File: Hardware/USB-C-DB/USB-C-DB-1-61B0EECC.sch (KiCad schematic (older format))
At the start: 5 parts

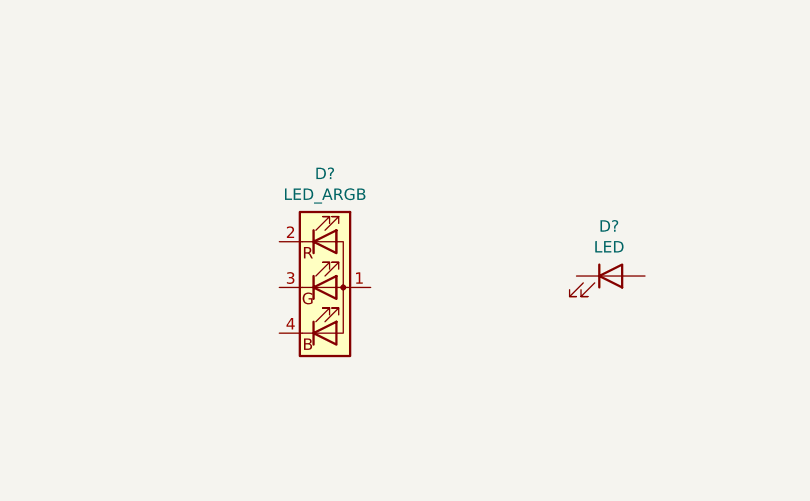
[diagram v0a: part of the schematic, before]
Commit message: Wiring up USB interface (schematic v0.3) > Adding ESD circuity for USB interface > Adding remaining bias and configuration circuity for the UBS interface IC
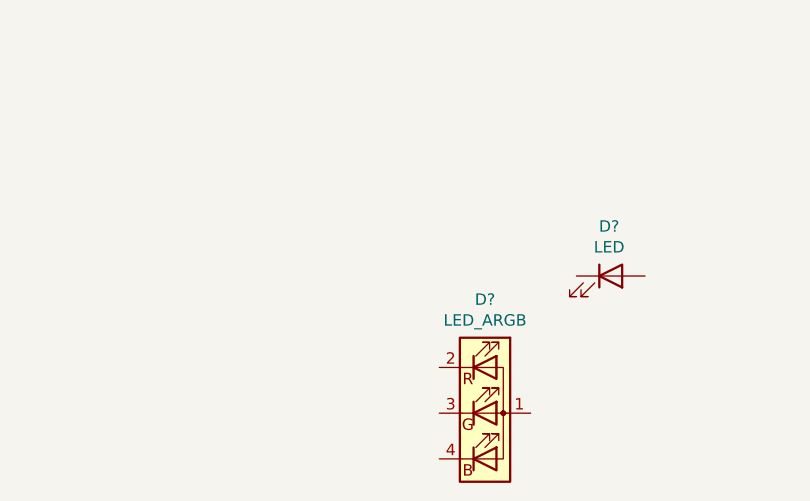
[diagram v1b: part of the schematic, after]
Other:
- moved on the sheet: D?
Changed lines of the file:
@@
 L Device:LED_ARGB D?
 U 1 1 61B13687
-P 4250 5550
+P 4950 6100
 AR Path="/61B13687" Ref="D?"  Part="1"
 AR Path="/61B0EECD/61B13687" Ref="D?"  Part="1"
-F 0 "D?" H 4250 6047 50  0000 C CNN
-F 1 "LED_ARGB" H 4250 5956 50  0000 C CNN
-F 2 "LED_SMD:LED_Cree-PLCC4_3.2x2.8mm_CCW" H 4250 5500 50  0001 C CNN
-F 3 "https://www.mouser.in/datasheet/2/723/CLV1L_FKB_1238-2583652.pdf" H 4250 5500 50  0001 C CNN
-F 4 "CLV1L-FKB-CJ1N1E1BB7B3B3" H 4250 5550 50  0001 C CNN "MPN"
-	1    4250 5550
+F 0 "D?" H 4950 6597 50  0000 C CNN
+F 1 "LED_ARGB" H 4950 6506 50  0000 C CNN
+F 2 "LED_SMD:LED_Cree-PLCC4_3.2x2.8mm_CCW" H 4950 6050 50  0001 C CNN
+F 3 "https://www.mouser.in/datasheet/2/723/CLV1L_FKB_1238-2583652.pdf" H 4950 6050 50  0001 C CNN
+F 4 "CLV1L-FKB-CJ1N1E1BB7B3B3" H 4950 6100 50  0001 C CNN "MPN"
+	1    4950 6100
 	1    0    0    -1
 $EndComp

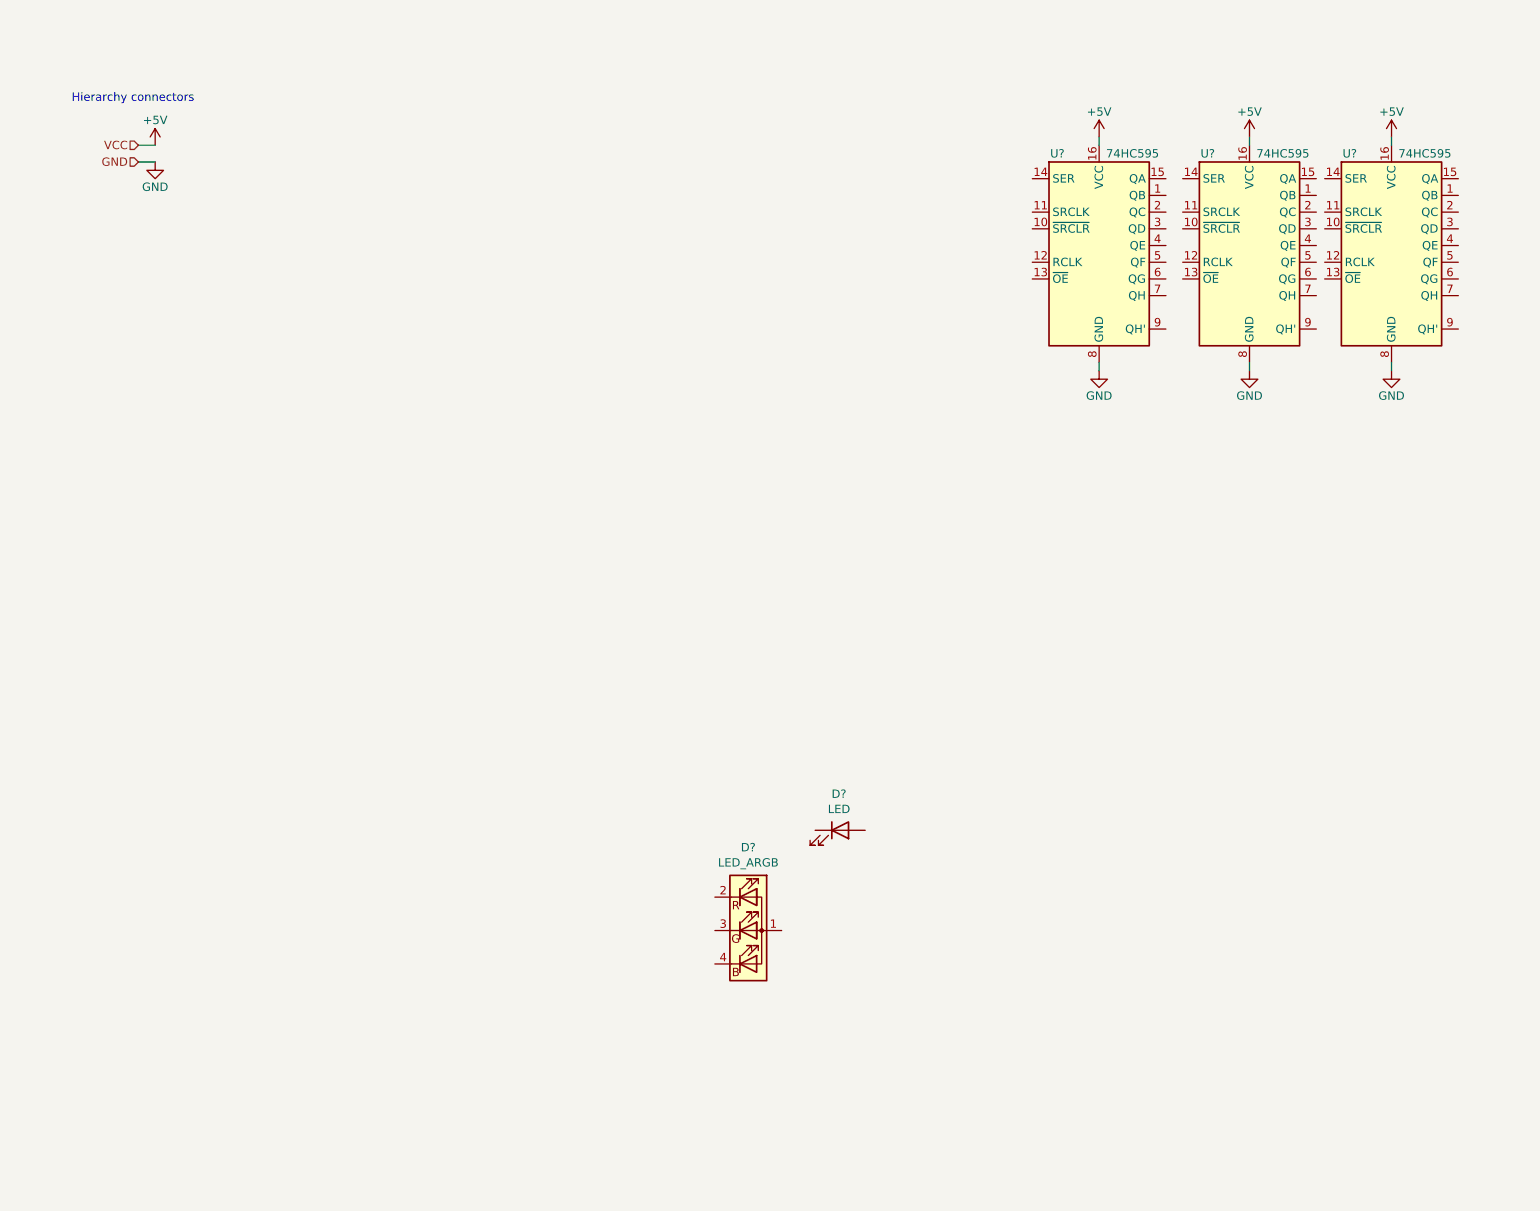
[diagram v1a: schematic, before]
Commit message: Adding PWM based brightness control circuit for display
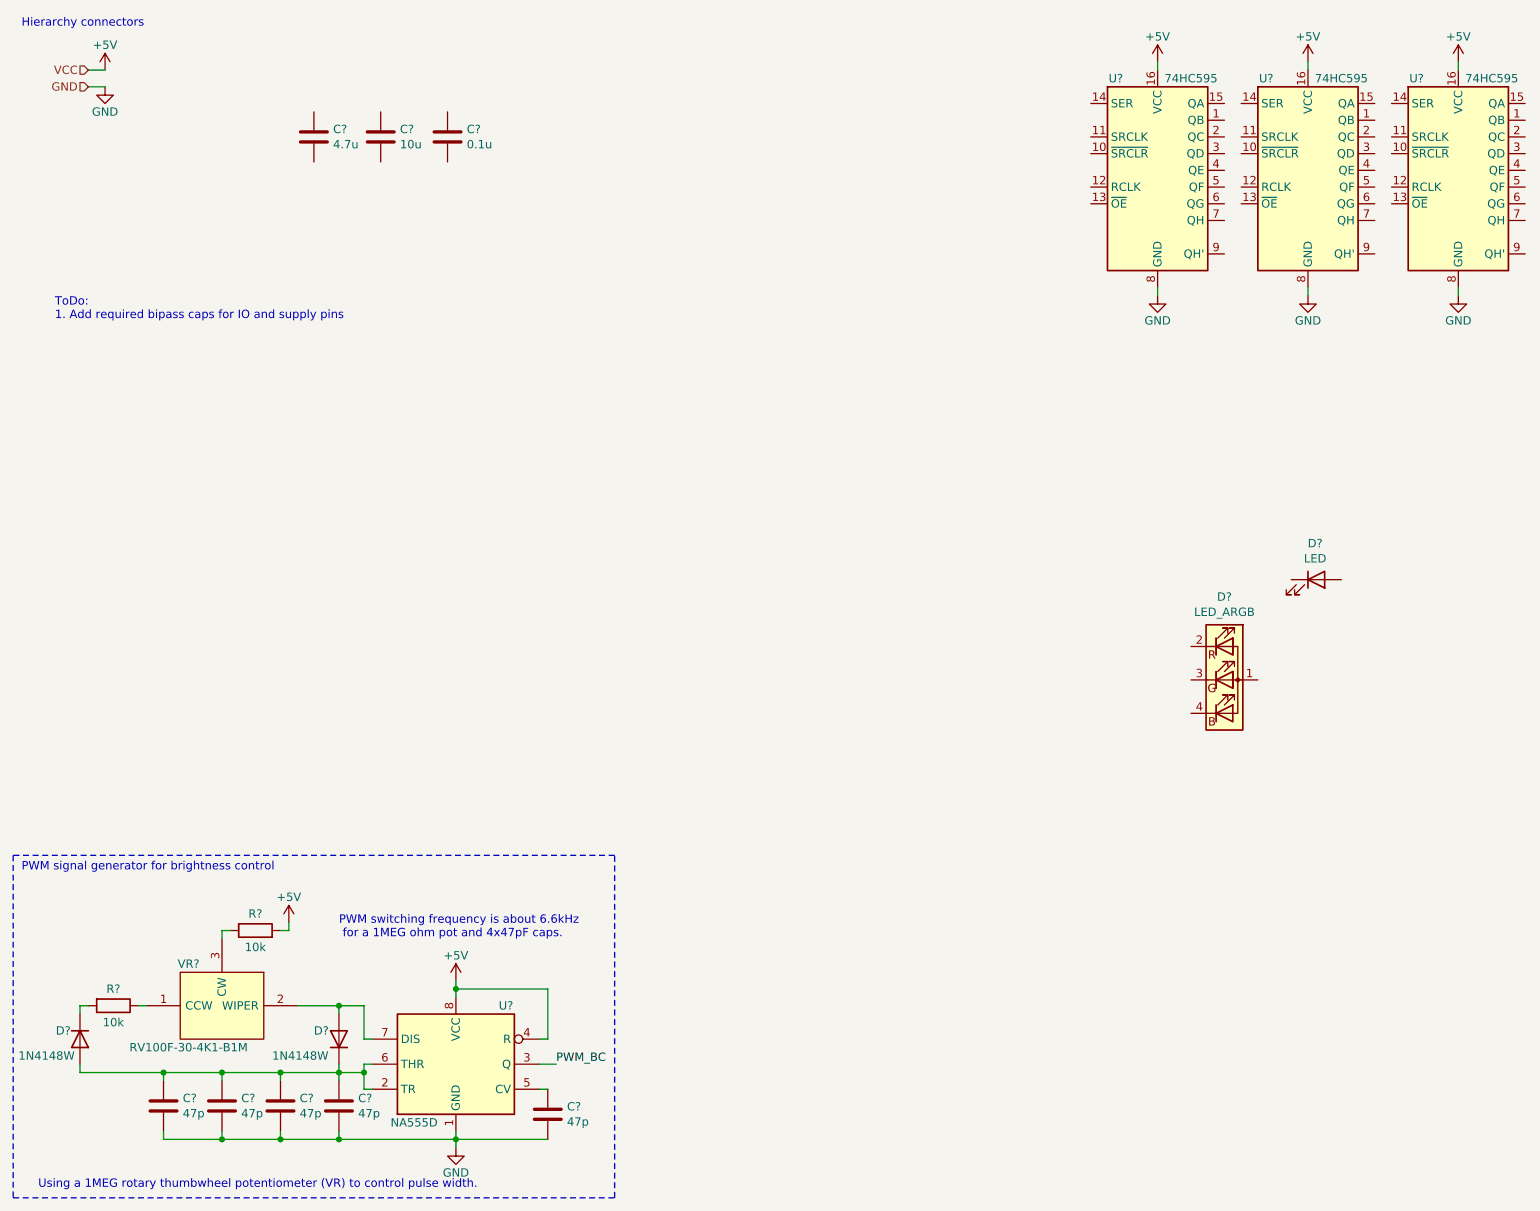
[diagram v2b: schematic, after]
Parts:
- added C?: 10u, Capacitor_SMD:C_0805_2012Metric_Pad1.18x1.45mm_HandSolder, symbol Device:C
- added C?: 0.1u, Capacitor_SMD:C_0805_2012Metric_Pad1.18x1.45mm_HandSolder, symbol Device:C
- added C?: 4.7u, Capacitor_SMD:C_0805_2012Metric_Pad1.18x1.45mm_HandSolder, symbol Device:C
- added C? (x5): 47p, Capacitor_SMD:C_0402_1005Metric_Pad0.74x0.62mm_HandSolder, symbol Device:C
- added D? (x2): 1N4148W, Diode_SMD:D_SOD-123, symbol Diode:1N4148W
- added R? (x2): 10k, Resistor_SMD:R_0603_1608Metric_Pad0.98x0.95mm_HandSolder, symbol Device:R
- added U?: NA555D, Package_SO:SOIC-8_3.9x4.9mm_P1.27mm, symbol USB-C-DB-rescue:NA555D
- added VR?: RV100F-30-4K1-B1M, RV100F304K1B1M, symbol USB-C-DB-rescue:RV100F-30-4K1-B1M
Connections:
- net +5V: now also R?.2, U?.4 (R), U?.8 (VCC)
- net GND: now also C?.2, C?.2, C?.2, C?.2, C?.2, U?.1 (GND)
- new net: R?.1, VR?.1 (CCW)
- new net: D?.2 (A), U?.7 (DIS), VR?.2 (WIPER)
- new net: R?.1, VR?.3 (CW)
- new net: C?.1, C?.1, C?.1, C?.1, D?.1 (K), D?.2 (A), U?.2 (TR), U?.6 (THR)
- new net: D?.1 (K), R?.2
- new net: C?.1, U?.5 (CV)
- new net PWM_BC: U?.3 (Q)
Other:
- note added: "PWM signal generator for brightness control"
- note added: "PWM switching frequency is about 6.6kHz\n for a 1MEG ohm pot and 4x47pF caps."
- note added: "ToDo:\n1. Add required bipass caps for IO and supply pins"
- note added: "Using a 1MEG rotary thumbwheel potentiometer (VR) to control pulse width."
- moved on the sheet: D?, U?

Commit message: Adding LED array to display subsection
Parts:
- removed U? (x2): 74HC595, Package_SO:TSSOP-16_4.4x5mm_P0.65mm, symbol 74xx:74HC595
- added C? (x7): 0.1u, Capacitor_SMD:C_0805_2012Metric_Pad1.18x1.45mm_HandSolder, symbol Device:C
- added C? (x7): 1u, Capacitor_SMD:C_0805_2012Metric_Pad1.18x1.45mm_HandSolder, symbol Device:C
- added D? (x87): LED_ARGB, LED_SMD:LED_Cree-PLCC4_3.2x2.8mm_CCW, symbol Device:LED_ARGB
- added Q? (x4): 2N7002KDW_R1_00001, SOT65P210X110-6N, symbol USB-C-DB-rescue:2N7002KDW_R1_00001
- added U? (x4): 74HC595, Package_SO:TSSOP-16_4.4x5mm_P0.65mm, symbol 74xx:74HC595
- added U?: 74HC595_mod, Package_SO:TSSOP-16_4.4x5mm_P0.65mm, symbol USB-C-DB-rescue:74HC595_mod
- U?: MPN (none) -> MC74HC595ADTG
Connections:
- net labels added: DATA, DCLK, EOUT, HSYNC, RESET, VSYNC
- wire segments 53 -> 1005
- no-connect marks 0 -> 2
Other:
- note added: "18-12-2021"
- note added: "Mini display board for testing and evaluating a USB Type-C interface for Micro-controllers."
- note added: "PWM switching frequency is about\n 6.6kHz for a 1MEG ohm pot and\n 4x47pF caps."
- note added: "USB-C demo board for Micro-controllers"
- note added: "v0.1"
- note removed: "PWM switching frequency is about 6.6kHz\n for a 1MEG ohm pot and 4x47pF caps."
- moved on the sheet: C?, D?, R?, U?, VR?

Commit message: Wiring up display subsection
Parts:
- removed C? (x2): 1u, Capacitor_SMD:C_0805_2012Metric_Pad1.18x1.45mm_HandSolder, symbol Device:C
- removed C?: 10u, Capacitor_SMD:C_0805_2012Metric_Pad1.18x1.45mm_HandSolder, symbol Device:C
- removed C? (x2): 0.1u, Capacitor_SMD:C_0805_2012Metric_Pad1.18x1.45mm_HandSolder, symbol Device:C
- removed C?: 4.7u, Capacitor_SMD:C_0805_2012Metric_Pad1.18x1.45mm_HandSolder, symbol Device:C
- removed D? (x8): LED_ARGB, LED_SMD:LED_Cree-PLCC4_3.2x2.8mm_CCW, symbol Device:LED_ARGB
- removed U?: 74HC595, Package_SO:TSSOP-16_4.4x5mm_P0.65mm, symbol 74xx:74HC595
- added D?: LED, LED_SMD:LED_Cree-PLCC4_3.2x2.8mm_CCW, symbol Device:LED
- added R? (x12): 309, Resistor_SMD:R_0603_1608Metric_Pad0.98x0.95mm_HandSolder, symbol Device:R
- added R? (x20): 583, Resistor_SMD:R_0603_1608Metric_Pad0.98x0.95mm_HandSolder, symbol Device:R
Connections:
- wire segments 1005 -> 1052
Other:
- note added: "23-02-2022"
- note added: "Debug LEDs\n (White)"
- note added: "LED power:\nRed - 1.9V @ 10mA (309 ohm)\nGreen - 1.5V @ 6mA (583 ohm)\nBlue - 1.5V @ 6mA (583 ohm)\nWorst case current draw: (10mA+6mA+6mA)*10 = 220mA"
- note added: "v0.2"
- note removed: "18-12-2021"
- note removed: "ToDo:\n1. Add required bipass caps for IO and supply pins"
- note removed: "v0.1"
- moved on the sheet: C?, D?, Q?, R?, U?, VR?

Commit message: Adding auto program functionality
> Adding OSHW logo to schematics
> Adding Test points for select signals
> Updating README with schematic images
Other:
- note added: "v0.3"
- note removed: "v0.2"
- moved on the sheet: C?, D?, Q?, R?, U?, VR?

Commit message: Cleaning up schematic after power budgeting
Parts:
- removed C?: 0.1u, Capacitor_SMD:C_0805_2012Metric_Pad1.18x1.45mm_HandSolder, symbol Device:C
- removed C? (x5): 47p, Capacitor_SMD:C_0402_1005Metric_Pad0.74x0.62mm_HandSolder, symbol Device:C
- removed D? (x2): 1N4148W, Diode_SMD:D_SOD-123, symbol Diode:1N4148W
- removed R? (x2): 10k, Resistor_SMD:R_0603_1608Metric_Pad0.98x0.95mm_HandSolder, symbol Device:R
- removed U?: NA555D, Package_SO:SOIC-8_3.9x4.9mm_P1.27mm, symbol USB-C-DB-rescue:NA555D
- removed VR?: RV100F-30-4K1-B1M, RV100F304K1B1M, symbol USB-C-DB-rescue:RV100F-30-4K1-B1M
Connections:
- net PWM_BC is gone; now on net +5V: Q?.3 (D2), Q?.3 (D2), Q?.3 (D2), Q?.3 (D2), Q?.6 (D1), Q?.6 (D1), Q?.6 (D1), Q?.6 (D1)
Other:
- note added: "LED power:\nRed - 1.9V @ 10mA (309 ohm @ 5V)\nGreen - 1.5V @ 6mA (583 ohm @ 5V)\nBlue - 1.5V @ 6mA (583 ohm @ 5V)\nWorst case current draw: (10mA+6mA+6mA)*10 = 220mA"
- note added: "Power budget:\nUSB interface: 23.6mA @ 5V\nMCU: 170mA @ 3.3V\nRegulator: 175mA @ 5V to 170mA @ 3.3V\nShift registers: 400uA @ 5V\nTimer: 6mA @ 5V\nLED drive: 220mA @ 5V\n\nDraw from USB connector at worst case: 425mA @ 5V (2.125W)\n"
- note added: "v0.4"
- note removed: "LED power:\nRed - 1.9V @ 10mA (309 ohm)\nGreen - 1.5V @ 6mA (583 ohm)\nBlue - 1.5V @ 6mA (583 ohm)\nWorst case current draw: (10mA+6mA+6mA)*10 = 220mA"
- note removed: "PWM signal generator for brightness control"
- note removed: "PWM switching frequency is about\n 6.6kHz for a 1MEG ohm pot and\n 4x47pF caps."
- note removed: "Using a 1MEG rotary thumbwheel potentiometer (VR) to control pulse width."
- note removed: "v0.3"

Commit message: Finalizing schematic for BOM analysis
* Replacing MOSFET parts with higher current version.
* Re-adding 555 based brightness control circuit.
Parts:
- removed Q? (x4): 2N7002KDW_R1_00001, SOT65P210X110-6N, symbol USB-C-DB-rescue:2N7002KDW_R1_00001
- added C?: 0.1u, Capacitor_SMD:C_0805_2012Metric_Pad1.18x1.45mm_HandSolder, symbol Device:C
- added C? (x5): 47p, Capacitor_SMD:C_0402_1005Metric_Pad0.74x0.62mm_HandSolder, symbol Device:C
- added D? (x2): 1N4148W, Diode_SMD:D_SOD-123, symbol Diode:1N4148W
- added J?: GND, TestPoint:TestPoint_Pad_D4.0mm, symbol Connector_Generic:Conn_01x01
- added J?: PWM_BC, TestPoint:TestPoint_Pad_D4.0mm, symbol Connector_Generic:Conn_01x01
- added J?: +5V, TestPoint:TestPoint_Pad_D4.0mm, symbol Connector_Generic:Conn_01x01
- added Q? (x8): XP262N7002TR-G, Package_TO_SOT_SMD:SOT-23, symbol USB-C-DB-rescue:XP262N7002TR-G
- added R? (x2): 10k, Resistor_SMD:R_0603_1608Metric_Pad0.98x0.95mm_HandSolder, symbol Device:R
- added U?: NA555D, Package_SO:SOIC-8_3.9x4.9mm_P1.27mm, symbol USB-C-DB-rescue:NA555D
- added VR?: RV100F-30-4K1-B1M, RV100F304K1B1M, symbol USB-C-DB-rescue:RV100F-30-4K1-B1M
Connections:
- net +5V: now also C?.1, J?.1 (Pin_1), R?.2, U?.4 (R), U?.8 (VCC)
- net GND: now also C?.2, C?.2, C?.2, C?.2, C?.2, C?.2, J?.1 (Pin_1), U?.1 (GND)
- net at D?.1 (A), D?.1 (A), D?.1 (A)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: now also Q?.2 (S) (x8)
- net at U?.15 (QA): now also Q?.1 (G)
- net at U?.1 (QB): now also Q?.1 (G)
- net at U?.2 (QC): now also Q?.1 (G)
- net at U?.3 (QD): now also Q?.1 (G)
- net at U?.4 (QE): now also Q?.1 (G)
- net at U?.5 (QF): now also Q?.1 (G)
- net at U?.6 (QG): now also Q?.1 (G)
- net at U?.7 (QH): now also Q?.1 (G)
- new net: R?.1, VR?.1 (CCW)
- new net: D?.2 (A), U?.7 (DIS), VR?.2 (WIPER)
- new net: R?.1, VR?.3 (CW)
- new net: C?.1, C?.1, C?.1, C?.1, D?.1 (K), D?.2 (A), U?.2 (TR), U?.6 (THR)
- new net: D?.1 (K), R?.2
- new net: C?.1, U?.5 (CV)
- new net PWM_BC: J?.1 (Pin_1), Q?.3 (D), Q?.3 (D), Q?.3 (D), Q?.3 (D), Q?.3 (D), Q?.3 (D), Q?.3 (D), Q?.3 (D), U?.3 (Q)
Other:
- note added: "11-03-2022"
- note added: "56mA max output load"
- note added: "60mA max output load"
- note added: "PWM signal generator for brightness control"
- note added: "PWM switching frequency is about\n 6.6kHz for a 1MEG ohm pot and\n 4x47pF caps."
- note added: "Power budget (worst case):\nUSB interface: 23.6mA @ 5V\nMCU: 170mA @ 3.3V (15mA during Modem-sleep)\nRegulator: 175mA @ 5V to 170mA @ 3.3V\nShift registers: 400uA @ 5V\nTimer: 6mA\nLED drive: 220mA @ 5V\n\nDraw from USB connector at worst case: 425mA @ 5V (2.125W)\nDraw from USB connector during MCU modem-sleep: 270mA @ 5V (1.35W)\n"
- note added: "Test points (bottom side)"
- note added: "Using MOSFETS cause the shift register cannot\n source/sink the currents needed by the LED array."
- note added: "Using a 1MEG rotary thumbwheel potentiometer (VR) to control pulse width."
- note added: "v0.5"
- note removed: "23-02-2022"
- note removed: "Power budget:\nUSB interface: 23.6mA @ 5V\nMCU: 170mA @ 3.3V\nRegulator: 175mA @ 5V to 170mA @ 3.3V\nShift registers: 400uA @ 5V\nTimer: 6mA @ 5V\nLED drive: 220mA @ 5V\n\nDraw from USB connector at worst case: 425mA @ 5V (2.125W)\n"
- note removed: "v0.4"

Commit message: Updating with alternative parts
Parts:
- C18, C20, C22, C24, C26, C32: renamed from C?; MPN1 (none) -> C0805C104M5RAC7800; MPN2 (none) -> C0805C104M5RACTU
- C27, C28, C29, C30, C31: renamed from C?; MPN1 (none) -> C0402C470J5GACTU
- J23, J24, J25: renamed from J?; footprint TestPoint:TestPoint_Pad_D4.0mm -> TestPoint:TestPoint_Pad_D1.0mm
- VR1: renamed from VR?; footprint RV100F304K1B1M -> Mouser-imports:RV100F304K1B1M; MPN1 (none) -> 3352W-1-105LF
- gave numbers to parts that had none: 137
